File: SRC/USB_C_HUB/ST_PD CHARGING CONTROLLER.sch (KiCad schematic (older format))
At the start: 16 parts, among them Q4 STL6P3LLH6, U13 STUSB4500QTR

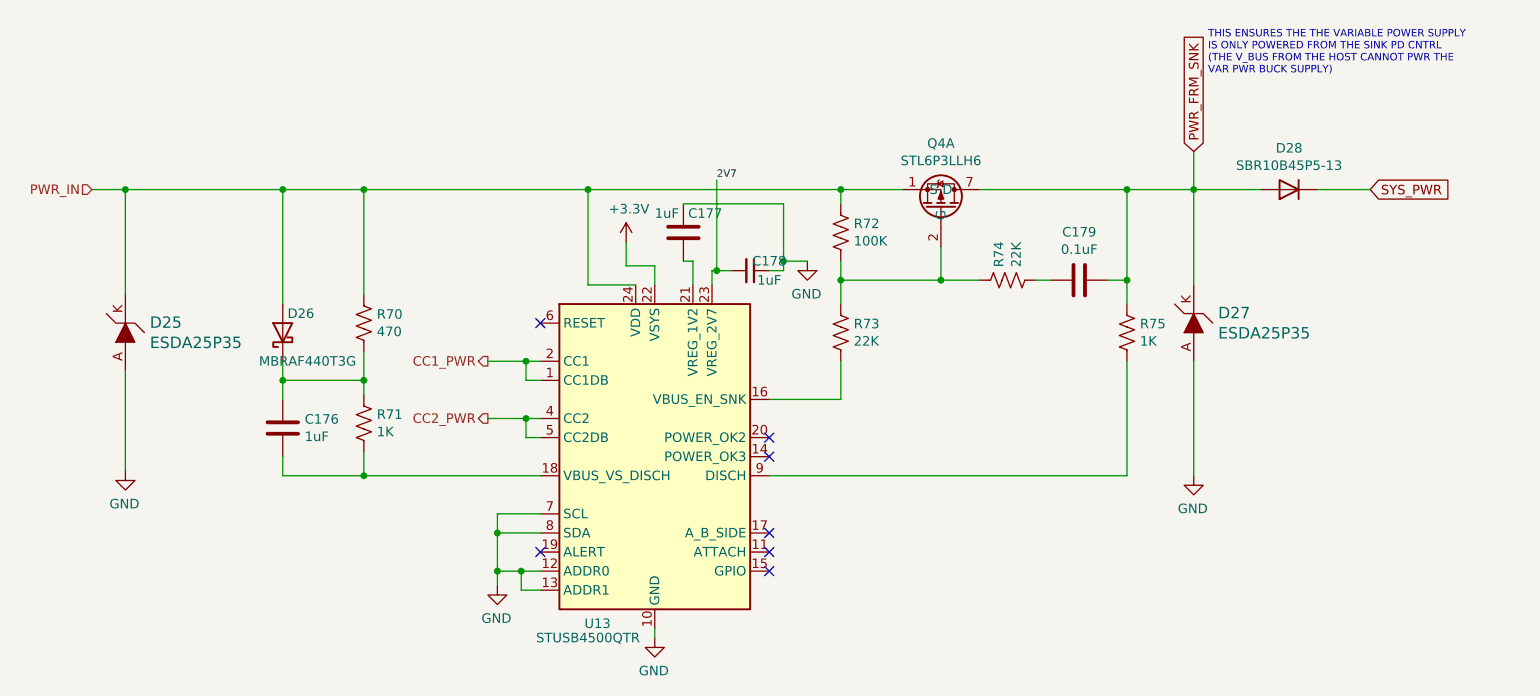
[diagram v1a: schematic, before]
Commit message: schematic capture and footprint assignment complete. Pending approval
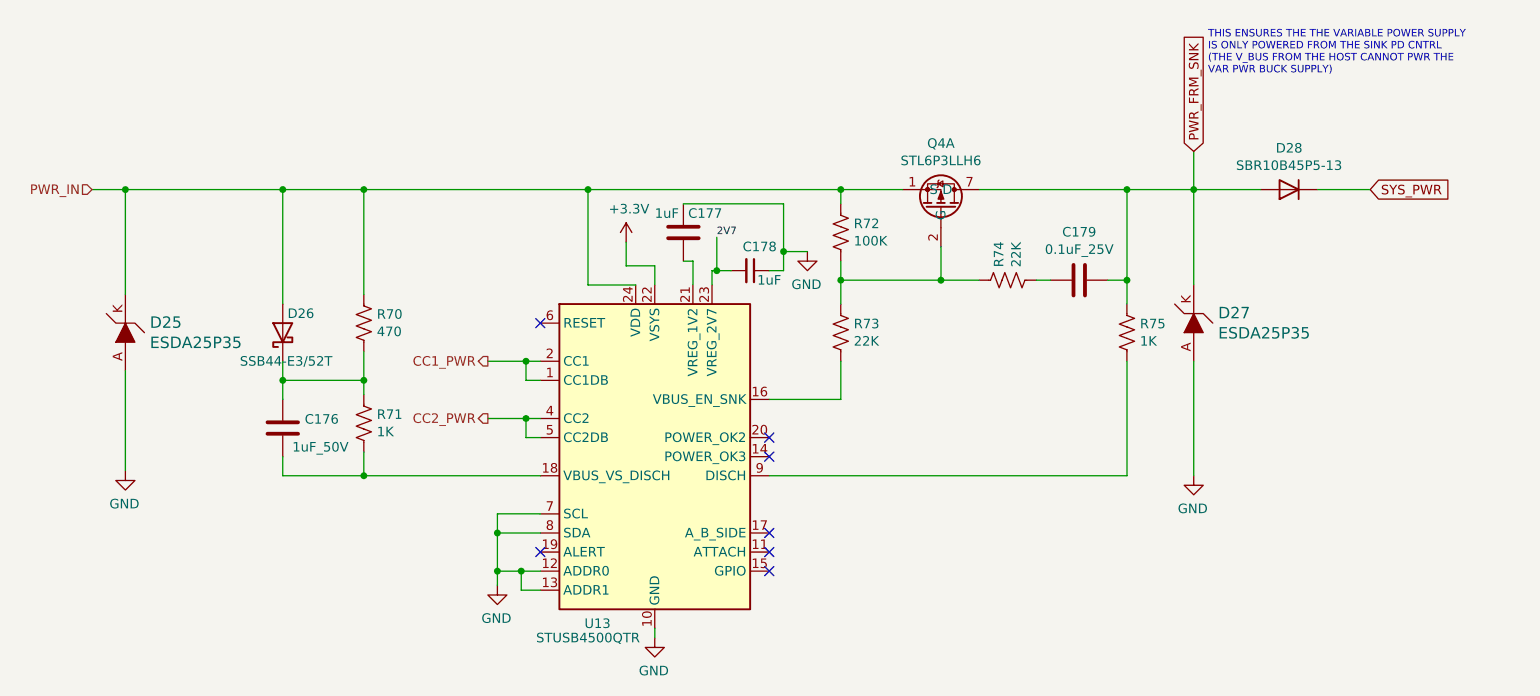
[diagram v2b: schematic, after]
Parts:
- C176: value 1uF -> 1uF_50V; footprint (none) -> Capacitor_SMD:C_0402_1005Metric; Mfr No. (none) -> CL05A105KA5NQNC
- C177, C178: footprint (none) -> Capacitor_SMD:C_0402_1005Metric
- C179: value 0.1uF -> 0.1uF_25V; footprint (none) -> Capacitor_SMD:C_0402_1005Metric; Mfr No. (none) -> GMC04X7R104K25NT
- D26: value MBRAF440T3G -> SSB44-E3/52T; footprint (none) -> Diode_SMD:D_SMB; Mfr No. (none) -> SSB44-E3/52T
- D27: Digi-Key_PN ESD5Z3.3T1GOSCT-ND -> (none); Vendor (none) -> LCSC
- D28: footprint (none) -> Diode_SMD:D_PowerDI-5; Vendor (none) -> DIgikey
- Q4: footprint (none) -> footprints:TRANS_STL6P3LLH6
- R70: footprint (none) -> Resistor_SMD:R_0603_1608Metric; Mfr No. (none) -> HPCR0603F470RK9
- R71: footprint (none) -> Resistor_SMD:R_0603_1608Metric; Mfr No. (none) -> ERJPB3D1001V
- R72: footprint (none) -> Resistor_SMD:R_0603_1608Metric; Mfr No. (none) -> HPCR0603F200KK9
- R73: footprint (none) -> Resistor_SMD:R_0603_1608Metric; Mfr No. (none) -> ERJP03J223V
- R74, R75: footprint (none) -> Resistor_SMD:R_0603_1608Metric
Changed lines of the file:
@@
 F 0 "R70" H 2868 2321 50  0000 L CNN
 F 1 "470" H 2868 2230 50  0000 L CNN
-F 2 "" V 2840 2265 50  0001 C CNN
+F 2 "Resistor_SMD:R_0603_1608Metric" V 2840 2265 50  0001 C CNN
 F 3 "~" H 2800 2275 50  0001 C CNN
+F 4 "HPCR0603F470RK9" H 2800 2275 50  0001 C CNN "Mfr No."
 	1    2800 2275
 	1    0    0    -1
@@
 AR Path="/61DDBD9F/61DE3B39" Ref="C176"  Part="1"
 F 0 "C176" H 2490 2871 50  0000 L CNN
-F 1 "1uF" H 2490 2780 50  0000 L CNN
-F 2 "" H 2413 2675 50  0001 C CNN
+F 1 "1uF_50V" H 2425 2725 50  0000 L CNN
+F 2 "Capacitor_SMD:C_0402_1005Metric" H 2413 2675 50  0001 C CNN
 F 3 "~" H 2375 2825 50  0001 C CNN
+F 4 " CL05A105KA5NQNC" H 2375 2825 50  0001 C CNN "Mfr No."
 	1    2375 2825
 	1    0    0    -1
@@
 F 0 "R71" H 2868 2846 50  0000 L CNN
 F 1 "1K" H 2868 2755 50  0000 L CNN
-F 2 "" V 2840 2790 50  0001 C CNN
+F 2 "Resistor_SMD:R_0603_1608Metric" V 2840 2790 50  0001 C CNN
 F 3 "~" H 2800 2800 50  0001 C CNN
+F 4 "ERJPB3D1001V" H 2800 2800 50  0001 C CNN "Mfr No."
 	1    2800 2800
 	1    0    0    -1
@@
 AR Path="/61DDBD9F/61DE3B46" Ref="D26"  Part="1"
 F 0 "D26" V 2475 2300 50  0000 R CNN
-F 1 "MBRAF440T3G" V 2225 2450 50  0000 R CNN
-F 2 "" H 2375 2325 50  0001 C CNN
+F 1 "SSB44-E3/52T" V 2225 2550 50  0000 R CNN
+F 2 "Diode_SMD:D_SMB" H 2375 2325 50  0001 C CNN
 F 3 "~" H 2375 2325 50  0001 C CNN
+F 4 "SSB44-E3/52T" V 2375 2325 50  0001 C CNN "Mfr No."
 	1    2375 2325
 	0    -1   -1   0
@@
 F 0 "Q4" V 6317 1325 50  0000 C CNN
 F 1 "STL6P3LLH6" V 6226 1325 50  0000 C CNN
-F 2 "" H 6075 1575 50  0001 C CNN
+F 2 "footprints:TRANS_STL6P3LLH6" H 6075 1575 50  0001 C CNN
 F 3 "" H 6075 1575 50  0001 C CNN
 	1    6075 1575
@@
 F 0 "R72" H 5368 1846 50  0000 L CNN
 F 1 "100K" H 5368 1755 50  0000 L CNN
-F 2 "" V 5340 1790 50  0001 C CNN
+F 2 "Resistor_SMD:R_0603_1608Metric" V 5340 1790 50  0001 C CNN
 F 3 "~" H 5300 1800 50  0001 C CNN
+F 4 "HPCR0603F200KK9" H 5300 1800 50  0001 C CNN "Mfr No."
 	1    5300 1800
 	1    0    0    -1
@@
 F 0 "R73" H 5368 2371 50  0000 L CNN
 F 1 "22K" H 5368 2280 50  0000 L CNN
-F 2 "" V 5340 2315 50  0001 C CNN
+F 2 "Resistor_SMD:R_0603_1608Metric" V 5340 2315 50  0001 C CNN
 F 3 "~" H 5300 2325 50  0001 C CNN
+F 4 "ERJP03J223V" H 5300 2325 50  0001 C CNN "Mfr No."
 	1    5300 2325
 	1    0    0    -1
@@
 F 0 "R74" H 6243 2096 50  0000 L CNN
 F 1 "22K" H 6243 2005 50  0000 L CNN
-F 2 "" V 6215 2040 50  0001 C CNN
+F 2 "Resistor_SMD:R_0603_1608Metric" V 6215 2040 50  0001 C CNN
 F 3 "~" H 6175 2050 50  0001 C CNN
 	1    6175 2050
@@
 AR Path="/61DDBD9F/61DE3B87" Ref="C179"  Part="1"
 F 0 "C179" V 6802 2050 50  0000 C CNN
-F 1 "0.1uF" V 6711 2050 50  0000 C CNN
-F 2 "" H 6588 1900 50  0001 C CNN
+F 1 "0.1uF_25V" V 6711 2050 50  0000 C CNN
+F 2 "Capacitor_SMD:C_0402_1005Metric" H 6588 1900 50  0001 C CNN
 F 3 "~" H 6550 2050 50  0001 C CNN
+F 4 "GMC04X7R104K25NT" V 6550 2050 50  0001 C CNN "Mfr No."
 	1    6550 2050
 	0    -1   -1   0
@@
 L OLIMEX_Power:GND #PWR?
 U 1 1 61DE3B95
-P 5125 1950
+P 5125 1900
 AR Path="/619540C6/61DE3B95" Ref="#PWR?"  Part="1"
 AR Path="/61DE3B95" Ref="#PWR?"  Part="1"
 AR Path="/61DDBD9F/61DE3B95" Ref="#PWR0169"  Part="1"
-F 0 "#PWR0169" H 5125 1700 50  0001 C CNN
-F 1 "GND" H 5130 1777 50  0000 C CNN
-F 2 "" H 5125 1950 60  0000 C CNN
-F 3 "" H 5125 1950 60  0000 C CNN
-	1    5125 1950
+F 0 "#PWR0169" H 5125 1650 50  0001 C CNN
+F 1 "GND" H 5130 1727 50  0000 C CNN
+F 2 "" H 5125 1900 60  0000 C CNN
+F 3 "" H 5125 1900 60  0000 C CNN
+	1    5125 1900
 	-1   0    0    -1
 $EndComp
@@
 AR Path="/61DE3B9B" Ref="C?"  Part="1"
 AR Path="/61DDBD9F/61DE3B9B" Ref="C178"  Part="1"
-F 0 "C178" V 4775 2100 50  0000 C CNN
+F 0 "C178" V 4700 2050 50  0000 C CNN
 F 1 "1uF" V 4875 2100 50  0000 C CNN
-F 2 "" H 4825 2000 50  0001 C CNN
+F 2 "Capacitor_SMD:C_0402_1005Metric" H 4825 2000 50  0001 C CNN
 F 3 "~" H 4825 2000 50  0001 C CNN
 	1    4825 2000
@@
 	4925 2000 5000 2000
 Wire Wire Line
-	5000 2000 5000 1950
-Wire Wire Line
-	5000 1950 5125 1950
-Wire Wire Line
-	5000 1650 5000 1950
-Connection ~ 5000 1950
+	5000 1900 5125 1900
+Wire Wire Line
+	5000 1650 5000 1900
 Wire Wire Line
 	4725 2000 4650 2000
@@
 F 0 "R75" H 6868 2371 50  0000 L CNN
 F 1 "1K" H 6868 2280 50  0000 L CNN
-F 2 "" V 6840 2315 50  0001 C CNN
+F 2 "Resistor_SMD:R_0603_1608Metric" V 6840 2315 50  0001 C CNN
 F 3 "~" H 6800 2325 50  0001 C CNN
 	1    6800 2325
@@
 F 2 "digikey-footprints:SOD-523" H 7350 2475 60  0001 L CNN
 F 3 "https://www.onsemi.com/pub/Collateral/ESD5Z2.5T1-D.PDF" H 7350 2575 60  0001 L CNN
-F 4 "ESD5Z3.3T1GOSCT-ND" H 7350 2675 60  0001 L CNN "Digi-Key_PN"
-F 5 "ESD5Z3.3T1G" H 7350 2775 60  0001 L CNN "MPN"
-F 6 "Circuit Protection" H 7350 2875 60  0001 L CNN "Category"
-F 7 "TVS - Diodes" H 7350 2975 60  0001 L CNN "Family"
-F 8 "https://www.onsemi.com/pub/Collateral/ESD5Z2.5T1-D.PDF" H 7350 3075 60  0001 L CNN "DK_Datasheet_Link"
-F 9 "/product-detail/en/on-semiconductor/ESD5Z3.3T1G/ESD5Z3.3T1GOSCT-ND/1967044" H 7350 3175 60  0001 L CNN "DK_Detail_Page"
-F 10 "TVS DIODE 3.3V 14.1V SOD523" H 7350 3275 60  0001 L CNN "Description"
-F 11 "ON Semiconductor" H 7350 3375 60  0001 L CNN "Manufacturer"
-F 12 "Active" H 7350 3475 60  0001 L CNN "Status"
+F 4 "ESD5Z3.3T1G" H 7350 2775 60  0001 L CNN "MPN"
+F 5 "Circuit Protection" H 7350 2875 60  0001 L CNN "Category"
+F 6 "TVS - Diodes" H 7350 2975 60  0001 L CNN "Family"
+F 7 "https://www.onsemi.com/pub/Collateral/ESD5Z2.5T1-D.PDF" H 7350 3075 60  0001 L CNN "DK_Datasheet_Link"
+F 8 "/product-detail/en/on-semiconductor/ESD5Z3.3T1G/ESD5Z3.3T1GOSCT-ND/1967044" H 7350 3175 60  0001 L CNN "DK_Detail_Page"
+F 9 "TVS DIODE 3.3V 14.1V SOD523" H 7350 3275 60  0001 L CNN "Description"
+F 10 "ON Semiconductor" H 7350 3375 60  0001 L CNN "Manufacturer"
+F 11 "Active" H 7350 3475 60  0001 L CNN "Status"
+F 12 "LCSC" V 7150 2275 50  0001 C CNN "Vendor"
 	1    7150 2275
 	0    -1   -1   0
@@
 F 0 "C177" H 4500 1900 50  0000 L CNN
 F 1 "1uF" H 4325 1900 50  0000 L CNN
-F 2 "" H 4513 1650 50  0001 C CNN
+F 2 "Capacitor_SMD:C_0402_1005Metric" H 4513 1650 50  0001 C CNN
 F 3 "~" H 4475 1800 50  0001 C CNN
 	1    4475 1800
 	1    0    0    -1
 $EndComp
-Text Label 4650 1525 0    39   ~ 0
+Text Label 4650 1825 0    39   ~ 0
 2V7
 Connection ~ 3975 1575
@@
 	4525 1950 4475 1950
 Wire Wire Line
-	4650 1525 4650 2000
+	4650 1825 4650 2000
 Wire Wire Line
 	4625 2075 4625 2000
@@
 U 1 1 61E1CE99
 P 7650 1575
+AR Path="/61DDBD9F/61E1CE99" Ref="D28"  Part="1"
+AR Path="/61EF7DEC/61E1CE99" Ref="D28"  Part="1"
 F 0 "D28" H 7650 1358 50  0000 C CNN
 F 1 "SBR10B45P5-13" H 7650 1449 50  0000 C CNN
-F 2 "" H 7650 1575 50  0001 C CNN
+F 2 "Diode_SMD:D_PowerDI-5" H 7650 1575 50  0001 C CNN
 F 3 "~" H 7650 1575 50  0001 C CNN
+F 4 "DIgikey" H 7650 1575 50  0001 C CNN "Vendor"
 	1    7650 1575
 	-1   0    0    1
@@
 Text HLabel 3450 2775 0    50   Output ~ 0
 CC2_PWR
+Connection ~ 5000 1900
+Wire Wire Line
+	5000 1900 5000 2000
 $EndSCHEMATC
